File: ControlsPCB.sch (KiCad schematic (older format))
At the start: 25 parts, among them J1 8P8C_Shielded, J2 8P8C_Shielded, U1 LTC4331IUFD-PBF, U3 LTC4331IUFD-PBF, U4 MCP23017-E_SP

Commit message: Switchbox Schematic Created
The nested schematic for the switchbox no exists using the 12V battery, LM2596 buck converter, and the MPC23017 I/O expander.
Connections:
- net +5V: now also U1.14 (SPEED1), U1.15 (SPEED2), U4.15 (A0), U4.16 (A1), U4.17 (A2)
- net Earth: no longer U4.15 (A0), U4.16 (A1), U4.17 (A2)
- net GND: no longer U1.14 (SPEED1)
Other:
- note added: "SPEED1 and SPEED2 are set to high in order to set the link rate at 12.5kHz\nwith a max cable length of 1200+ meters. Other combinations of how these two \npins are set will allow different speeds and different max extension lengths. \nThis designated "speed index" must be set the same on both local and remote LTC4331s"
- note removed: "SPEED1 is set to low and SPEED2 to float in order to set the link rate at 125kHz\nwith a max cable length of 600 meters. Other combinations of how these two \npins are set will allow different speeds and different max extension lengths. \nThis designated "speed index" must be set the same on both sides."
- moved on the sheet: R6, R7, R8
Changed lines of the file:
@@
 Text GLabel 3250 2600 2    50   Input ~ 0
 SDA1
-$Comp
-L 2020-09-01_04-44-37:LTC4331IUFD-PBF U1
-U 1 1 5F4E03B4
-P 5100 2000
-F 0 "U1" H 6100 2387 60  0000 C CNN
-F 1 "LTC4331IUFD-PBF" H 6100 2281 60  0000 C CNN
-F 2 "QFN_20_ADI" H 6100 2240 60  0001 C CNN
-F 3 "" H 5100 2000 60  0000 C CNN
-	1    5100 2000
-	1    0    0    -1
-$EndComp
 Wire Wire Line
 	5100 2200 5100 2100
@@
 	-1   0    0    1
 $EndComp
-Wire Wire Line
-	4600 2700 5100 2700
-Wire Wire Line
-	4250 2600 5100 2600
 Connection ~ 5000 2900
-Wire Wire Line
-	5000 2900 5100 2900
 $Comp
 L power:+5V #PWR?
@@
 	4250 2600 4200 2600
 Connection ~ 4250 2600
-$Comp
-L power:GND #PWR?
-U 1 1 5F5786CF
-P 7100 2700
-F 0 "#PWR?" H 7100 2450 50  0001 C CNN
-F 1 "GND" V 7105 2572 50  0000 R CNN
-F 2 "" H 7100 2700 50  0001 C CNN
-F 3 "" H 7100 2700 50  0001 C CNN
-	1    7100 2700
-	0    -1   -1   0
-$EndComp
-Text Notes 9050 1100 2    50   ~ 0
-SPEED1 is set to low and SPEED2 to float in order to set the link rate at 125kHz\nwith a max cable length of 600 meters. Other combinations of how these two \npins are set will allow different speeds and different max extension lengths. \nThis designated "speed index" must be set the same on both sides.
+Text Notes 5850 950  0    50   ~ 0
+SPEED1 and SPEED2 are set to high in order to set the link rate at 12.5kHz\nwith a max cable length of 1200+ meters. Other combinations of how these two \npins are set will allow different speeds and different max extension lengths. \nThis designated "speed index" must be set the same on both local and remote LTC4331s
 $Comp
 L 2020-09-01_04-44-37:LTC4331IUFD-PBF U3
@@
 L power:+5V #PWR?
 U 1 1 5F57F945
-P 7100 2400
-F 0 "#PWR?" H 7100 2250 50  0001 C CNN
-F 1 "+5V" V 7115 2528 50  0000 L CNN
-F 2 "" H 7100 2400 50  0001 C CNN
-F 3 "" H 7100 2400 50  0001 C CNN
-	1    7100 2400
-	0    1    1    0
-$EndComp
-Wire Wire Line
-	4500 2100 5100 2100
+P 7800 2600
+F 0 "#PWR?" H 7800 2450 50  0001 C CNN
+F 1 "+5V" V 7815 2728 50  0000 L CNN
+F 2 "" H 7800 2600 50  0001 C CNN
+F 3 "" H 7800 2600 50  0001 C CNN
+	1    7800 2600
+	1    0    0    -1
+$EndComp
 Wire Wire Line
 	4500 1700 4500 1800
-Connection ~ 5100 2100
 $Comp
 L power:+5V #PWR?
@@
 L power:GND #PWR?
 U 1 1 5F5892C8
-P 7100 2500
-F 0 "#PWR?" H 7100 2250 50  0001 C CNN
-F 1 "GND" V 7105 2372 50  0000 R CNN
-F 2 "" H 7100 2500 50  0001 C CNN
-F 3 "" H 7100 2500 50  0001 C CNN
-	1    7100 2500
-	0    -1   -1   0
+P 7600 2400
+F 0 "#PWR?" H 7600 2150 50  0001 C CNN
+F 1 "GND" V 7605 2272 50  0000 R CNN
+F 2 "" H 7600 2400 50  0001 C CNN
+F 3 "" H 7600 2400 50  0001 C CNN
+	1    7600 2400
+	1    0    0    -1
 $EndComp
 Text Notes 5100 1100 2    50   ~ 0
 Bypass Capacitors
-Text GLabel 8000 2200 2    50   Input ~ 0
-B
-Text GLabel 8250 2500 2    50   Input ~ 0
-A
-Wire Wire Line
-	7100 2200 7700 2200
-Text Notes 8200 2350 0    50   ~ 0
-A, B, and Vcc are \ncarried by a \nCAT5 cable 100m
 Text GLabel 9800 5400 2    50   Input ~ 0
 A
@@
 $Comp
 L power:Earth #PWR?
-U 1 1 5F5DF504
-P 4400 6100
-F 0 "#PWR?" H 4400 5850 50  0001 C CNN
-F 1 "Earth" H 4400 5950 50  0001 C CNN
-F 2 "" H 4400 6100 50  0001 C CNN
-F 3 "~" H 4400 6100 50  0001 C CNN
-	1    4400 6100
-	1    0    0    -1
-$EndComp
-Connection ~ 4400 6100
-$Comp
-L power:Earth #PWR?
 U 1 1 5F5E5B08
 P 1900 5700
@@
 	-1   0    0    1
 $EndComp
-Wire Wire Line
-	4650 2400 5100 2400
 $Comp
 L Device:R_US R9
@@
 Wire Wire Line
 	6350 5500 6800 5500
-$Comp
-L Device:R_US R8
-U 1 1 5F5F92E4
-P 7700 2650
-F 0 "R8" H 7632 2604 50  0000 R CNN
-F 1 "620" H 7632 2695 50  0000 R CNN
-F 2 "" V 7740 2640 50  0001 C CNN
-F 3 "~" H 7700 2650 50  0001 C CNN
-	1    7700 2650
-	-1   0    0    1
-$EndComp
-$Comp
-L power:+5V #PWR?
-U 1 1 5F5F92EA
-P 7700 2800
-F 0 "#PWR?" H 7700 2650 50  0001 C CNN
-F 1 "+5V" V 7715 2928 50  0000 L CNN
-F 2 "" H 7700 2800 50  0001 C CNN
-F 3 "" H 7700 2800 50  0001 C CNN
-	1    7700 2800
-	-1   0    0    1
-$EndComp
-Wire Wire Line
-	8250 2500 7850 2500
-Wire Wire Line
-	7550 2300 7100 2300
-$Comp
-L Device:R_US R7
-U 1 1 5F5FE91B
-P 7850 2350
-F 0 "R7" H 7782 2304 50  0000 R CNN
-F 1 "110" H 7782 2395 50  0000 R CNN
-F 2 "" V 7890 2340 50  0001 C CNN
-F 3 "~" H 7850 2350 50  0001 C CNN
-	1    7850 2350
-	-1   0    0    1
-$EndComp
-Wire Wire Line
-	7550 2500 7550 2300
-Connection ~ 7850 2500
-$Comp
-L Device:R_US R6
-U 1 1 5F60224B
-P 7700 2050
-F 0 "R6" H 7632 2004 50  0000 R CNN
-F 1 "620" H 7632 2095 50  0000 R CNN
-F 2 "" V 7740 2040 50  0001 C CNN
-F 3 "~" H 7700 2050 50  0001 C CNN
-	1    7700 2050
-	-1   0    0    1
-$EndComp
-$Comp
-L power:GND #PWR?
-U 1 1 5F602751
-P 7700 1900
-F 0 "#PWR?" H 7700 1650 50  0001 C CNN
-F 1 "GND" H 7705 1727 50  0000 C CNN
-F 2 "" H 7700 1900 50  0001 C CNN
-F 3 "" H 7700 1900 50  0001 C CNN
-	1    7700 1900
-	-1   0    0    1
-$EndComp
-Connection ~ 7700 2500
-Wire Wire Line
-	7700 2500 7550 2500
-Wire Wire Line
-	7700 2500 7850 2500
-Connection ~ 7700 2200
-Wire Wire Line
-	7700 2200 7850 2200
 Text GLabel 5900 5700 0    50   Input ~ 0
 SCL2
@@
 Connection ~ 6800 5200
 Connection ~ 6400 4950
-Connection ~ 7850 2200
-Wire Wire Line
-	7850 2200 8000 2200
-$Sheet
-S 850  1100 600  800
-U 5F57B52C
-F0 "SWITCHBOX" 50
-F1 "switchbox.sch" 50
-F2 "SCL1" I R 1450 1300 50
-$EndSheet
 $Comp
 L Connector:Conn_01x08_Male J?
@@
 Wire Wire Line
 	4850 5800 4400 5800
+$Sheet
+S 850  1100 600  800
+U 5F57B52C
+F0 "SWITCHBOX" 50
+F1 "switchbox.sch" 50
+F2 "SCL1" I R 1450 1400 50
+F3 "SDA1" I R 1450 1300 50
+$EndSheet
+$Comp
+L power:+5V #PWR?
+U 1 1 5F763441
+P 4550 6100
+F 0 "#PWR?" H 4550 5950 50  0001 C CNN
+F 1 "+5V" H 4565 6273 50  0000 C CNN
+F 2 "" H 4550 6100 50  0001 C CNN
+F 3 "" H 4550 6100 50  0001 C CNN
+	1    4550 6100
+	1    0    0    -1
+$EndComp
+Wire Wire Line
+	4400 6100 4550 6100
+Connection ~ 4400 6100
+$Comp
+L power:+5V #PWR?
+U 1 1 5F76A721
+P 7450 2300
+F 0 "#PWR?" H 7450 2150 50  0001 C CNN
+F 1 "+5V" V 7465 2428 50  0000 L CNN
+F 2 "" H 7450 2300 50  0001 C CNN
+F 3 "" H 7450 2300 50  0001 C CNN
+	1    7450 2300
+	1    0    0    -1
+$EndComp
+Wire Wire Line
+	8450 1650 8600 1650
+Connection ~ 8450 1650
+Wire Wire Line
+	8300 1650 8450 1650
+Connection ~ 8300 1650
+Wire Wire Line
+	8300 1950 8450 1950
+Connection ~ 8300 1950
+$Comp
+L power:GND #PWR?
+U 1 1 5F602751
+P 8300 1350
+F 0 "#PWR?" H 8300 1100 50  0001 C CNN
+F 1 "GND" H 8305 1177 50  0000 C CNN
+F 2 "" H 8300 1350 50  0001 C CNN
+F 3 "" H 8300 1350 50  0001 C CNN
+	1    8300 1350
+	-1   0    0    1
+$EndComp
+$Comp
+L Device:R_US R6
+U 1 1 5F60224B
+P 8300 1500
+F 0 "R6" H 8232 1454 50  0000 R CNN
+F 1 "620" H 8232 1545 50  0000 R CNN
+F 2 "" V 8340 1490 50  0001 C CNN
+F 3 "~" H 8300 1500 50  0001 C CNN
+	1    8300 1500
+	-1   0    0    1
+$EndComp
+Connection ~ 8450 1950
+$Comp
+L Device:R_US R7
+U 1 1 5F5FE91B
+P 8450 1800
+F 0 "R7" H 8382 1754 50  0000 R CNN
+F 1 "110" H 8382 1845 50  0000 R CNN
+F 2 "" V 8490 1790 50  0001 C CNN
+F 3 "~" H 8450 1800 50  0001 C CNN
+	1    8450 1800
+	-1   0    0    1
+$EndComp
+Wire Wire Line
+	8850 1950 8450 1950
+$Comp
+L power:+5V #PWR?
+U 1 1 5F5F92EA
+P 8300 2250
+F 0 "#PWR?" H 8300 2100 50  0001 C CNN
+F 1 "+5V" V 8315 2378 50  0000 L CNN
+F 2 "" H 8300 2250 50  0001 C CNN
+F 3 "" H 8300 2250 50  0001 C CNN
+	1    8300 2250
+	-1   0    0    1
+$EndComp
+$Comp
+L Device:R_US R8
+U 1 1 5F5F92E4
+P 8300 2100
+F 0 "R8" H 8232 2054 50  0000 R CNN
+F 1 "620" H 8232 2145 50  0000 R CNN
+F 2 "" V 8340 2090 50  0001 C CNN
+F 3 "~" H 8300 2100 50  0001 C CNN
+	1    8300 2100
+	-1   0    0    1
+$EndComp
+Text Notes 8800 1800 0    50   ~ 0
+A, B, and Vcc are \ncarried by a \nCAT5 cable 100m
+Text GLabel 8850 1950 2    50   Input ~ 0
+A
+Text GLabel 8600 1650 2    50   Input ~ 0
+B
+Wire Wire Line
+	5000 2900 5100 2900
+Wire Wire Line
+	4600 2700 5100 2700
+Wire Wire Line
+	4250 2600 5100 2600
+Wire Wire Line
+	4650 2400 5100 2400
+Wire Wire Line
+	4500 2100 5100 2100
+Wire Wire Line
+	7250 2200 7250 1650
+Wire Wire Line
+	7250 1650 8300 1650
+Wire Wire Line
+	7300 2300 7300 1950
+Wire Wire Line
+	7300 1950 8300 1950
+Wire Wire Line
+	7450 2400 7450 2300
+Connection ~ 5100 2100
+Wire Wire Line
+	7100 2400 7450 2400
+Wire Wire Line
+	7100 2300 7300 2300
+Wire Wire Line
+	7100 2200 7250 2200
+$Comp
+L 2020-09-01_04-44-37:LTC4331IUFD-PBF U1
+U 1 1 5F4E03B4
+P 5100 2000
+F 0 "U1" H 6100 2387 60  0000 C CNN
+F 1 "LTC4331IUFD-PBF" H 6100 2281 60  0000 C CNN
+F 2 "QFN_20_ADI" H 6100 2240 60  0001 C CNN
+F 3 "" H 5100 2000 60  0000 C CNN
+	1    5100 2000
+	1    0    0    -1
+$EndComp
+Wire Wire Line
+	7100 2500 7500 2500
+Wire Wire Line
+	7500 2500 7500 2400
+Wire Wire Line
+	7500 2400 7600 2400
+Wire Wire Line
+	7100 2600 7100 2700
+Wire Wire Line
+	7100 2700 7800 2700
+Wire Wire Line
+	7800 2700 7800 2600
+Connection ~ 7100 2700
+Text GLabel 1450 1400 2    50   Input ~ 0
+SCL1
+Text GLabel 1450 1300 2    50   Input ~ 0
+SDA1
 $EndSCHEMATC

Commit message: Local Master Nested and Formatted
Local Master(Arduino and Local Slace LTC4331) was placed in a nested sheet. Grounds were changed to face down and power was oriented upwards.
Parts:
- removed A1: Arduino_UNO_R2, Module:Arduino_UNO_R2, symbol MCU_Module:Arduino_UNO_R2
- removed C1: 4.7uF, symbol Device:C
- removed C2: 1uF, symbol Device:C
- removed D1: LED, symbol Device:LED
- removed R2: 10k, symbol Device:R_US
- removed R3, R4: 2.7k, symbol Device:R_US
- removed R5: 1.5k, symbol Device:R_US
- removed R6, R8: 620, symbol Device:R_US
- removed R7: 110, symbol Device:R_US
- removed U1: LTC4331IUFD-PBF, QFN_20_ADI, symbol 2020-09-01_04-44-37:LTC4331IUFD-PBF
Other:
- note added: "Never let SLO pin on LTC4331 float."
- note removed: "Bypass Capacitors"
- note removed: "Keep C1 \nwithin 7mm \nof Vcc pin"
- note removed: "Local Slave"
- note removed: "Never let SLO float."
- note removed: "SPEED1 and SPEED2 are set to high in order to set the link rate at 12.5kHz\nwith a max cable length of 1200+ meters. Other combinations of how these two \npins are set will allow different speeds and different max extension lengths. \nThis designated "speed index" must be set the same on both local and remote LTC4331s"

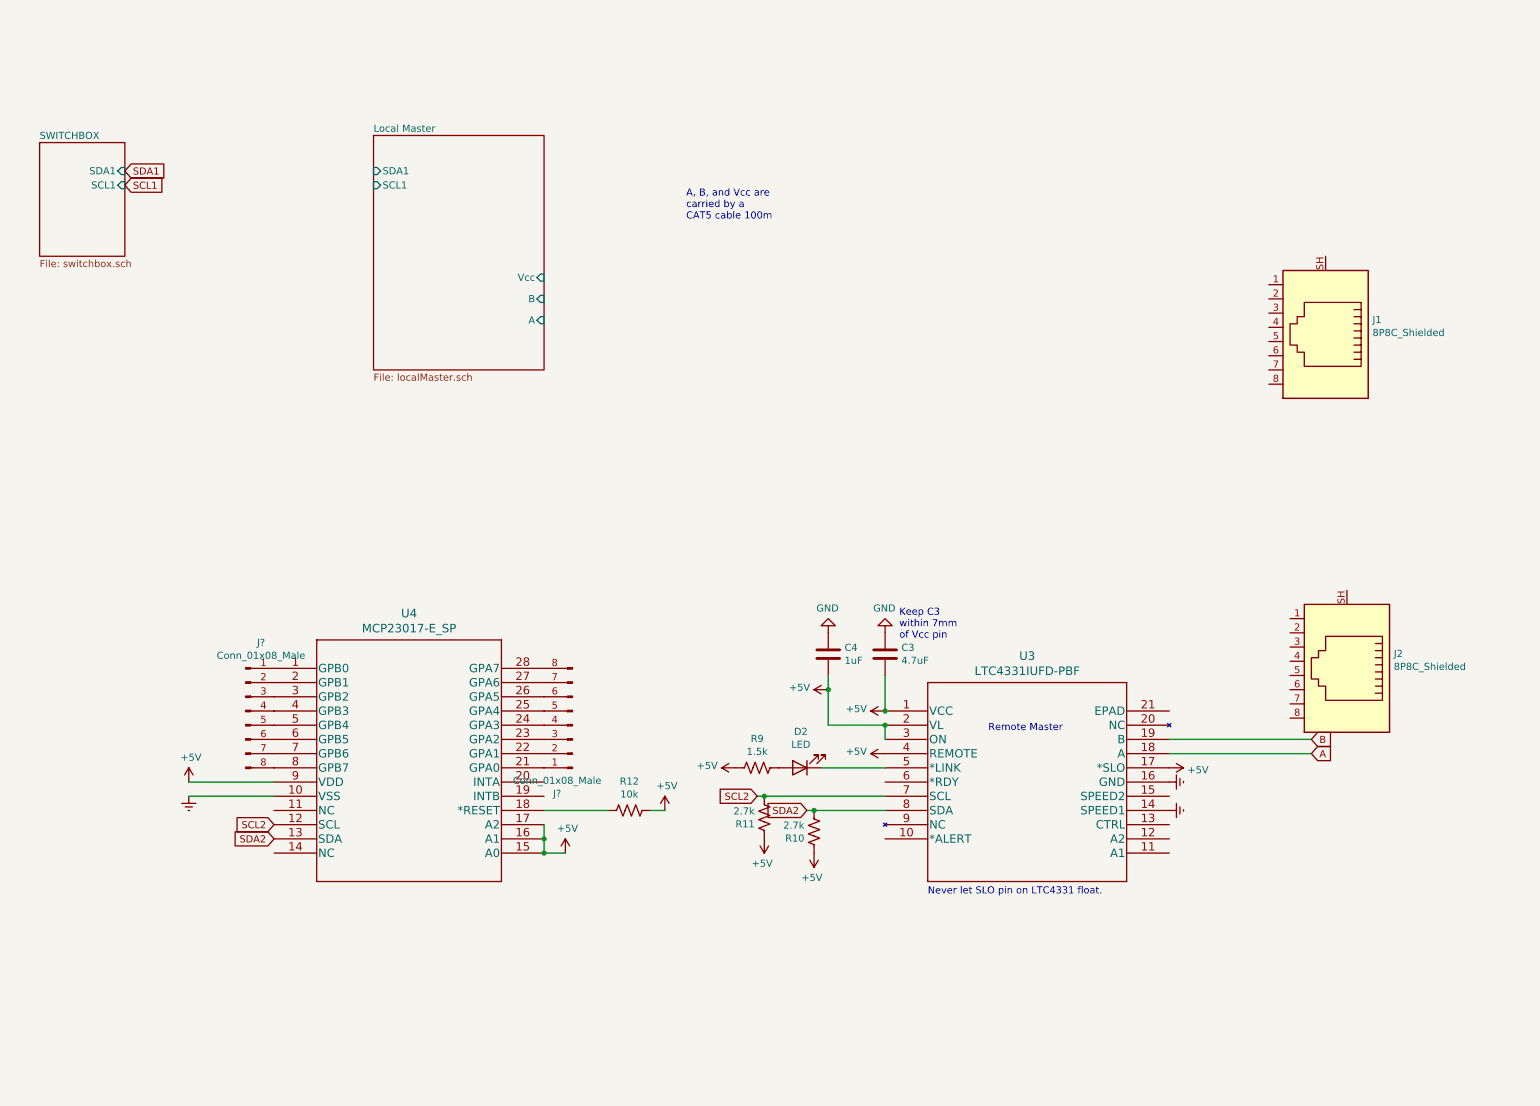
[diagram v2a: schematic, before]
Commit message: Remote Master Connections and Fixes
Remote Master(LTC4331 and MPC23017 in Controls Box) were nested and connections were made. Ground facing down and power facing up was also added.
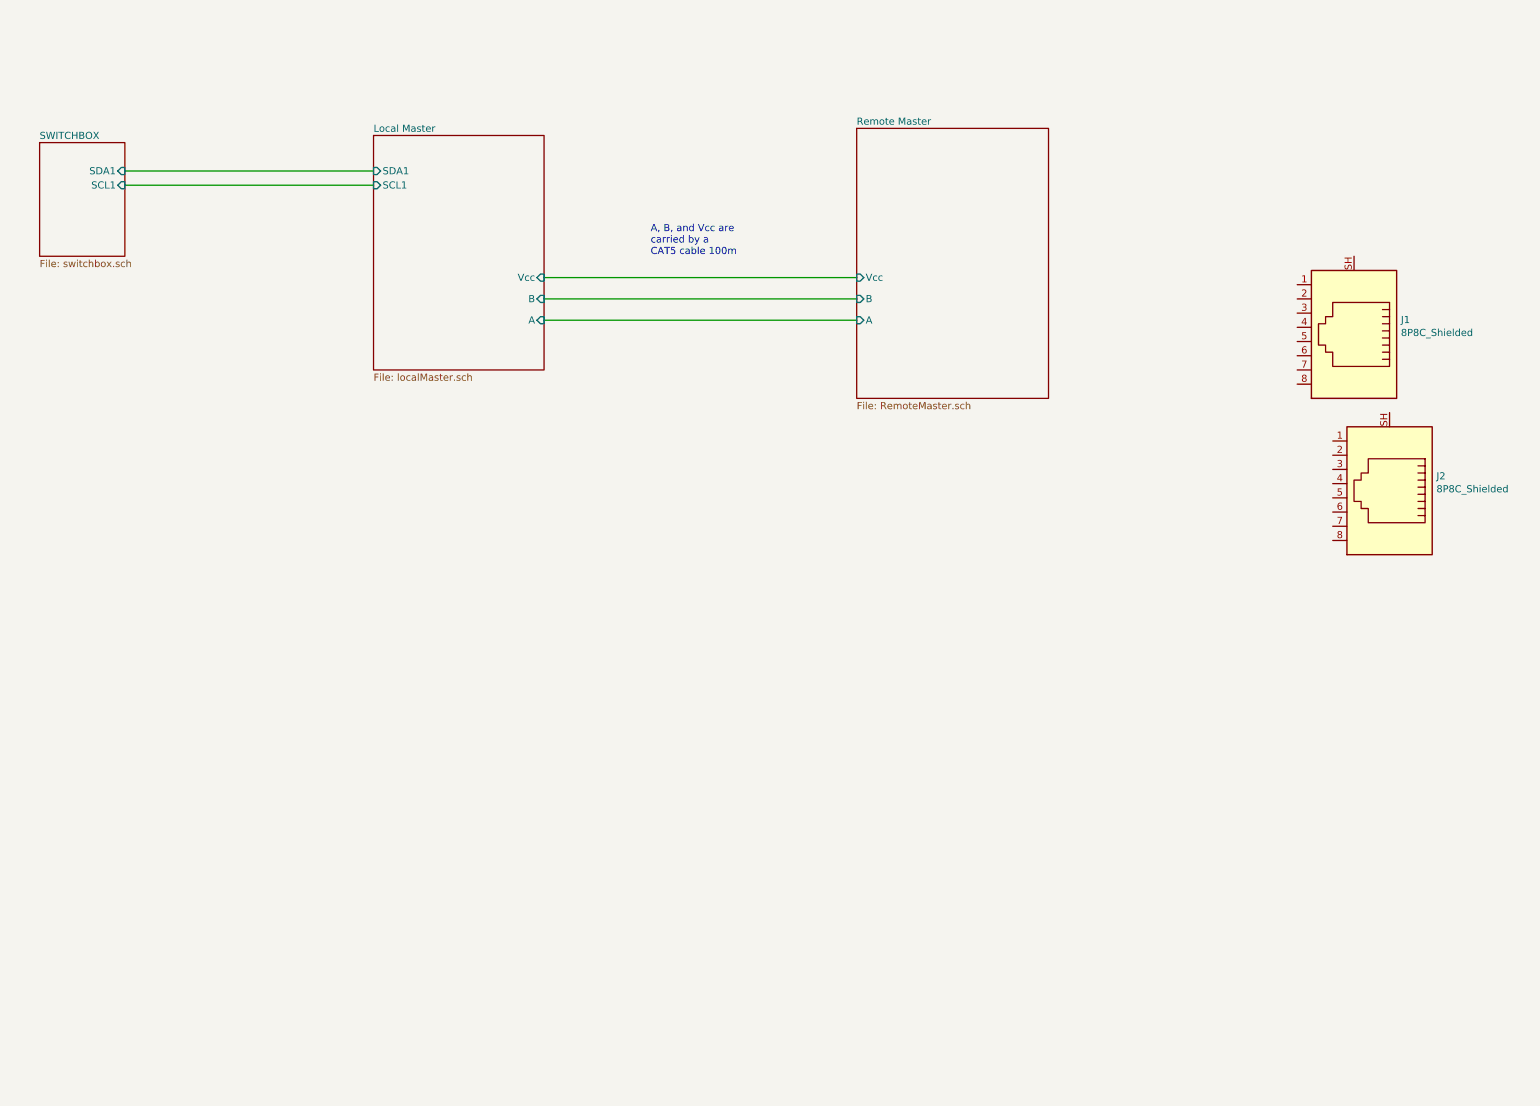
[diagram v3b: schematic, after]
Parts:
- removed C3: 4.7uF, symbol Device:C
- removed C4: 1uF, symbol Device:C
- removed D2: LED, symbol Device:LED
- removed J? (x2): Conn_01x08_Male, symbol Connector:Conn_01x08_Male
- removed R10, R11: 2.7k, symbol Device:R_US
- removed R12: 10k, symbol Device:R_US
- removed R9: 1.5k, symbol Device:R_US
- removed U3: LTC4331IUFD-PBF, QFN_20_ADI, symbol 2020-09-01_04-44-37:LTC4331IUFD-PBF
- removed U4: MCP23017-E_SP, SPDIP28_300MC_MCH, symbol 2020-09-01_02-26-45:MCP23017-E_SP
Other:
- note removed: "Keep C3\nwithin 7mm \nof Vcc pin"
- note removed: "Never let SLO pin on LTC4331 float."
- note removed: "Remote Master"
- moved on the sheet: J1, J2

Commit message: publish jeff review
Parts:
- added A?: Arduino_UNO_R2, Module:Arduino_UNO_R2, symbol MCU_Module:Arduino_UNO_R2
- added BT? (x2): Battery_Cell, symbol Device:Battery_Cell
- added U? (x2): LM2596S-ADJ, Package_TO_SOT_SMD:TO-263-5_TabPin3, symbol Regulator_Switching:LM2596S-ADJ
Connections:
- net LOCAL_TRANSCEIVER/B: now reaches J1.1
- net LOCAL_TRANSCEIVER/B: now also J2.1
- net LOCAL_TRANSCEIVER/A: now reaches J1.2
- net LOCAL_TRANSCEIVER/A: now also J2.2
- net GND: now reaches J1.8
- net GND: now also J2.8, A?.29 (GND), A?.6 (GND), A?.7 (GND), BT?.2 (-), BT?.2 (-), U?.2 (OUT), U?.2 (OUT), U?.3 (GND), U?.3 (GND), U?.5 (~ON~/OFF), U?.5 (~ON~/OFF)
- new net: BT?.1 (+), U?.1 (VIN) (x2)
- new net +5V: U?.4 (FB), U?.4 (FB)
- new net LOCAL_TRANSCEIVER/SCL: A?.14 (SCL/A5)
- new net LOCAL_TRANSCEIVER/SDA: A?.13 (SDA/A4)
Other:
- note added: "12V"
- note added: "Both systems will lie roughly\n100yd ~~ 100m apart.\n\nGrounds will be shared"
- note added: "Buck converter is\nexternal to our system"
- note removed: "A, B, and Vcc are \ncarried by a \nCAT5 cable 100m"
- moved on the sheet: J1, J2
